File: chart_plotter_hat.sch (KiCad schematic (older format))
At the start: 65 parts, among them J1 JST PH, J10 JST PH, J2 JST PH, J3 40HAT, J4 JST PH, J5 JST PH, J6 JST PH, J7 JST PH, J8 Conn_02x03_Odd_Even, J9 JST PH, Q1 DMG2305UX, Q2 DMMT5401, Q3 DMG2305UX, U1 ATmega328P-AU, U2 CAT24C32, U3 MPM3610-5.0-adafruit, U4 LT1762-3.3, U5 G3VM-201FR, U6 MCP2515-xSO, U7 MCP2551-I-SN, U8 ST2378E, Y1 16MHz

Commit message: Added optical isolation in CAN
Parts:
- removed D1, D2: LED, LEDs:LED_0603, symbol Device:LED
- removed H5, H6: LightPipeMount, project_footprints:SMFLPX.X-light-pipe-adapter-smd, symbol CustomComponents:LightPipeMount
- removed J2: JST PH, Connectors_JST:JST_PH_B4B-PH-K_04x2.00mm_Straight, symbol Connector_Generic:Conn_01x04
- removed R3: 120, Resistors_SMD:R_0603, symbol Device:R
- removed R4: 300, Resistors_SMD:R_0603, symbol Device:R
- added C8, C9: .1uF, Capacitors_SMD:C_0603, symbol Device:C
- added J2: JST PH, Connectors_JST:JST_PH_B6B-PH-K_06x2.00mm_Straight, symbol Connector_Generic:Conn_01x06
- added U9: ADuM1201BR, Housings_SOIC:SOIC-8_3.9x4.9mm_Pitch1.27mm, symbol Isolator:ADuM1201BR
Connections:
- net labels added: LED_ACTION
- wire segments 245 -> 254
- no-connect marks 12 -> 23
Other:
- moved on the sheet: C12, C15, U7

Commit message: Redid CAN isolation, removed level shifter
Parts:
- removed C10: .1uF, Capacitors_SMD:C_0603, symbol Device:C
- removed Q3: DMG2305UX, TO_SOT_Packages_SMD:SOT-23, symbol raspberrypi_hat:DMG2305UX
- removed R12, R15, R5: 10K, Resistors_SMD:R_0603, symbol Device:R
- removed R14: 220, Resistors_SMD:R_0603, symbol Device:R
- removed U8: ST2378E, Housings_SSOP:TSSOP-20_4.4x6.5mm_Pitch0.65mm, symbol CustomComponents:ST2378E
- added C10: 10uF, Capacitors_Tantalum_SMD:CP_Tantalum_Case-A_EIA-3216-18_Reflow, symbol Device:CP
- added U8: LT1762-MS8, Housings_SSOP:MSOP-8_3x3mm_Pitch0.65mm, symbol CustomComponents:LT1762-MS8
- C11: value .1uF -> .01uF
- R11, R13, R16: value 10K -> 6.8K
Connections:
- net labels added: +5VP, GND2
- net labels removed: CCS, CRST, INT, MISO-2, MOSI-2, SCK-2, VEE_ENABLE
- wire segments 254 -> 225
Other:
- note added: "CAN Isolated Power"
- note removed: "3.3V Auxiliary"
- note removed: "VEE_ENABLE is active low to power auxiliary"
- moved on the sheet: C12, C15, C16, C17, C8, C9, J10, R11, R13, R16, U6, U7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

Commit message: Updated README
Created pdf of schematic, updated board graphic
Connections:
- net GND2 is gone; now on net GND: C10.2, C15.2, C9.2, U7.2 (VSS), U7.8 (Rs), U8.4 (GND), U8.7 (NC), U9.5 (GND2)
- net EN: no longer U8.5 (SHDN)
- net GND: now also U1.1 (PD3)
- net CAN_EN: now reaches U1.9 (PD5)
- net CAN_EN: now also U8.5 (SHDN)
- net CS renamed AVR_CS
- net LED_ACTION renamed LED1
- no-connect marks 23 -> 21
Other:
- note added: "HDWR IDENT"
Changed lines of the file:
@@
 	13100 5925 13375 5925
 Text GLabel 13375 5625 2    50   Input ~ 0
-CS
+AVR_CS
 Wire Wire Line
 	13100 5525 14950 5525
@@
 	2050 2375 1750 2375
 Text GLabel 3575 2375 2    50   Output ~ 0
-CS
+AVR_CS
 Wire Wire Line
 	3250 2375 3575 2375
@@
 MCU_RUNNING
 $Comp
-L Device:R R1
-U 1 1 5FEF7011
-P 14225 7575
-F 0 "R1" V 14305 7575 50  0000 C CNN
-F 1 "10K" V 14225 7575 50  0000 C CNN
-F 2 "Resistors_SMD:R_0603" V 14155 7575 50  0001 C CNN
-F 3 "" H 14225 7575 50  0001 C CNN
-	1    14225 7575
-	0    1    1    0
-$EndComp
-$Comp
-L power:+3.3V #PWR013
-U 1 1 5FF4180B
-P 14600 7575
-F 0 "#PWR013" H 14600 7425 50  0001 C CNN
-F 1 "+3.3V" H 14615 7748 50  0000 C CNN
-F 2 "" H 14600 7575 50  0001 C CNN
-F 3 "" H 14600 7575 50  0001 C CNN
-	1    14600 7575
-	1    0    0    -1
-$EndComp
-$Comp
 L Device:C C5
 U 1 1 5FFED6E8
@@
 	1750 3075 2050 3075
 NoConn ~ 13100 7725
-NoConn ~ 13100 7625
-NoConn ~ 13100 7425
 NoConn ~ 13100 7225
 NoConn ~ 13100 7125
@@
 $EndComp
 Text GLabel 14525 4500 0    50   Output ~ 0
-LED_ACTION
+LED1
 Text GLabel 13675 5425 2    50   Output ~ 0
-LED_ACTION
+LED1
 Wire Wire Line
 	13100 5425 13675 5425
@@
 L power:+5VP #PWR017
 U 1 1 612C4211
-P 6950 6600
-F 0 "#PWR017" H 6950 6450 50  0001 C CNN
-F 1 "+5VP" H 6965 6773 50  0000 C CNN
-F 2 "" H 6950 6600 50  0001 C CNN
-F 3 "" H 6950 6600 50  0001 C CNN
-	1    6950 6600
+P 7125 6600
+F 0 "#PWR017" H 7125 6450 50  0001 C CNN
+F 1 "+5VP" H 7140 6773 50  0000 C CNN
+F 2 "" H 7125 6600 50  0001 C CNN
+F 3 "" H 7125 6600 50  0001 C CNN
+	1    7125 6600
 	1    0    0    -1
 $EndComp
@@
 	6950 6900 6950 7350
 Text GLabel 5125 7000 0    50   Input ~ 0
-EN
+CAN_EN
 Wire Wire Line
 	5125 7000 5250 7000
@@
 Wire Wire Line
 	6050 7350 6950 7350
+$Comp
+L power:GND2 #PWR0127
+U 1 1 6123FC34
+P 14625 4600
+F 0 "#PWR0127" H 14625 4350 50  0001 C CNN
+F 1 "GND2" H 14630 4427 50  0000 C CNN
+F 2 "" H 14625 4600 50  0001 C CNN
+F 3 "" H 14625 4600 50  0001 C CNN
+	1    14625 4600
+	1    0    0    -1
+$EndComp
+Wire Wire Line
+	14625 4600 14850 4600
+Connection ~ 14850 4600
+Text GLabel 13375 7625 2    50   Output ~ 0
+CAN_EN
+Wire Wire Line
+	13100 7625 13375 7625
+$Comp
+L power:+3.3V #PWR013
+U 1 1 5FF4180B
+P 14600 7575
+F 0 "#PWR013" H 14600 7425 50  0001 C CNN
+F 1 "+3.3V" H 14615 7748 50  0000 C CNN
+F 2 "" H 14600 7575 50  0001 C CNN
+F 3 "" H 14600 7575 50  0001 C CNN
+	1    14600 7575
+	1    0    0    -1
+$EndComp
+$Comp
+L Device:R R1
+U 1 1 5FEF7011
+P 14225 7575
+F 0 "R1" V 14305 7575 50  0000 C CNN
+F 1 "10K" V 14225 7575 50  0000 C CNN
+F 2 "Resistors_SMD:R_0603" V 14155 7575 50  0001 C CNN
+F 3 "" H 14225 7575 50  0001 C CNN
+	1    14225 7575
+	0    1    1    0
+$EndComp
+Text Notes 13425 7425 0    50   ~ 0
+HDWR IDENT
+$Comp
+L power:GND #PWR?
+U 1 1 612417F0
+P 13925 7425
+F 0 "#PWR?" H 13925 7175 50  0001 C CNN
+F 1 "GND" H 13925 7275 50  0000 C CNN
+F 2 "" H 13925 7425 50  0000 C CNN
+F 3 "" H 13925 7425 50  0000 C CNN
+	1    13925 7425
+	1    0    0    -1
+$EndComp
+Wire Wire Line
+	13100 7425 13925 7425
+Wire Wire Line
+	6950 6600 7125 6600
 $EndSCHEMATC

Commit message: Added power isolation to CAN
TVS added to CAN output
DCP01B used for power isolation from board
Another LT1762 used for CAN isolation power
Removed pull-ups from CAN controller, should be controlled by Pi
Added LED's for hat pwr, pi pwr, CAN isolation pwr, and CAN Rx
Reordered connections on Power connector
Added CAN gnd isolation pin on CAN connector
No more CAN_EN, as it is covered by isolation hookup
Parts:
- removed J10: JST PH, Connectors_JST:JST_PH_B2B-PH-K_02x2.00mm_Straight, symbol Connector_Generic:Conn_01x02
- removed R11, R13, R16: 6.8K, Resistors_SMD:R_0603, symbol Device:R
- added C13: 1uF, Capacitors_SMD:C_1206, symbol Device:C
- added C14: 2.2uF, Capacitors_SMD:C_1206, symbol Device:C
- added D2, D3, D4: RED, Diodes_SMD:D_0603, symbol Device:LED
- added D5: GRN, Diodes_SMD:D_0603, symbol Device:LED
- added J10: JST PH, Connectors_JST:JST_PH_B3B-PH-K_03x2.00mm_Straight, symbol Connector_Generic:Conn_01x03
- added R12: 300, Resistors_SMD:R_0603, symbol Device:R
- added R3, R5: 390, Resistors_SMD:R_0603, symbol Device:R
- added R4: 180, Resistors_SMD:R_0603, symbol Device:R
- added U10: DCP01B, CustomComponents:DCP01B_SO_7_14, symbol CustomComponents:DCP01B
- added U11: VCAN26A2, TO_SOT_Packages_SMD:SOT-323_SC-70, symbol CustomComponents:VCAN26A2
- renumbered D3 to D1
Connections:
- net +12V: no longer U8.8 (Vin)
- net +3V3: now also D3.2 (A)
- net +5V: now also J2.3 (Pin_3), J2.5 (Pin_5), C14.1, D2.2 (A), U10.1 (Vs); no longer J2.2 (Pin_2), J2.4 (Pin_4)
- net +5VP: now also D4.2 (A)
- net BUTTON: now also J2.4 (Pin_4); no longer J2.3 (Pin_3)
- net CAN_HI: now also J10.1 (Pin_1), U11.2
- net CAN_LO: now also J10.2 (Pin_2), U11.1
- net GND: now also J2.2 (Pin_2), C14.2, R3.1, R4.1, U10.2 (0V); no longer C10.2, C15.2, C9.2, J2.6 (Pin_6), U7.2 (VSS), U7.8 (Rs), U8.4 (GND), U8.7 (NC), U9.5 (GND2)
- net LED1: now also J2.6 (Pin_6); no longer J2.5 (Pin_5)
- net at U7.4 (RXD), U9.7 (VIA): now also D5.2 (A)
- net CAN_EN: no longer names the net of U1.9 (PD5)
- net CAN_EN: no longer U8.5 (SHDN)
- new net: C13.1, U10.6 (Vout), U8.5 (SHDN), U8.8 (Vin)
- new net: D2.1 (K), R3.2
- new net: D3.1 (K), R4.2
- new net: D4.1 (K), R5.2
- new net: D5.1 (K), R12.2
- new net GND2: C10.2, C13.2, C15.2, C9.2, J10.3 (Pin_3), R12.1, R5.1, U10.5 (0V), U11.3, U7.2 (VSS), U7.8 (Rs), U8.4 (GND), U9.5 (GND2)
- no-connect marks 21 -> 25
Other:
- note added: "CAN Connector"
- moved on the sheet: C10, C11, C12, C15, C16, C17, C8, C9, U6, U7, U8, U9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

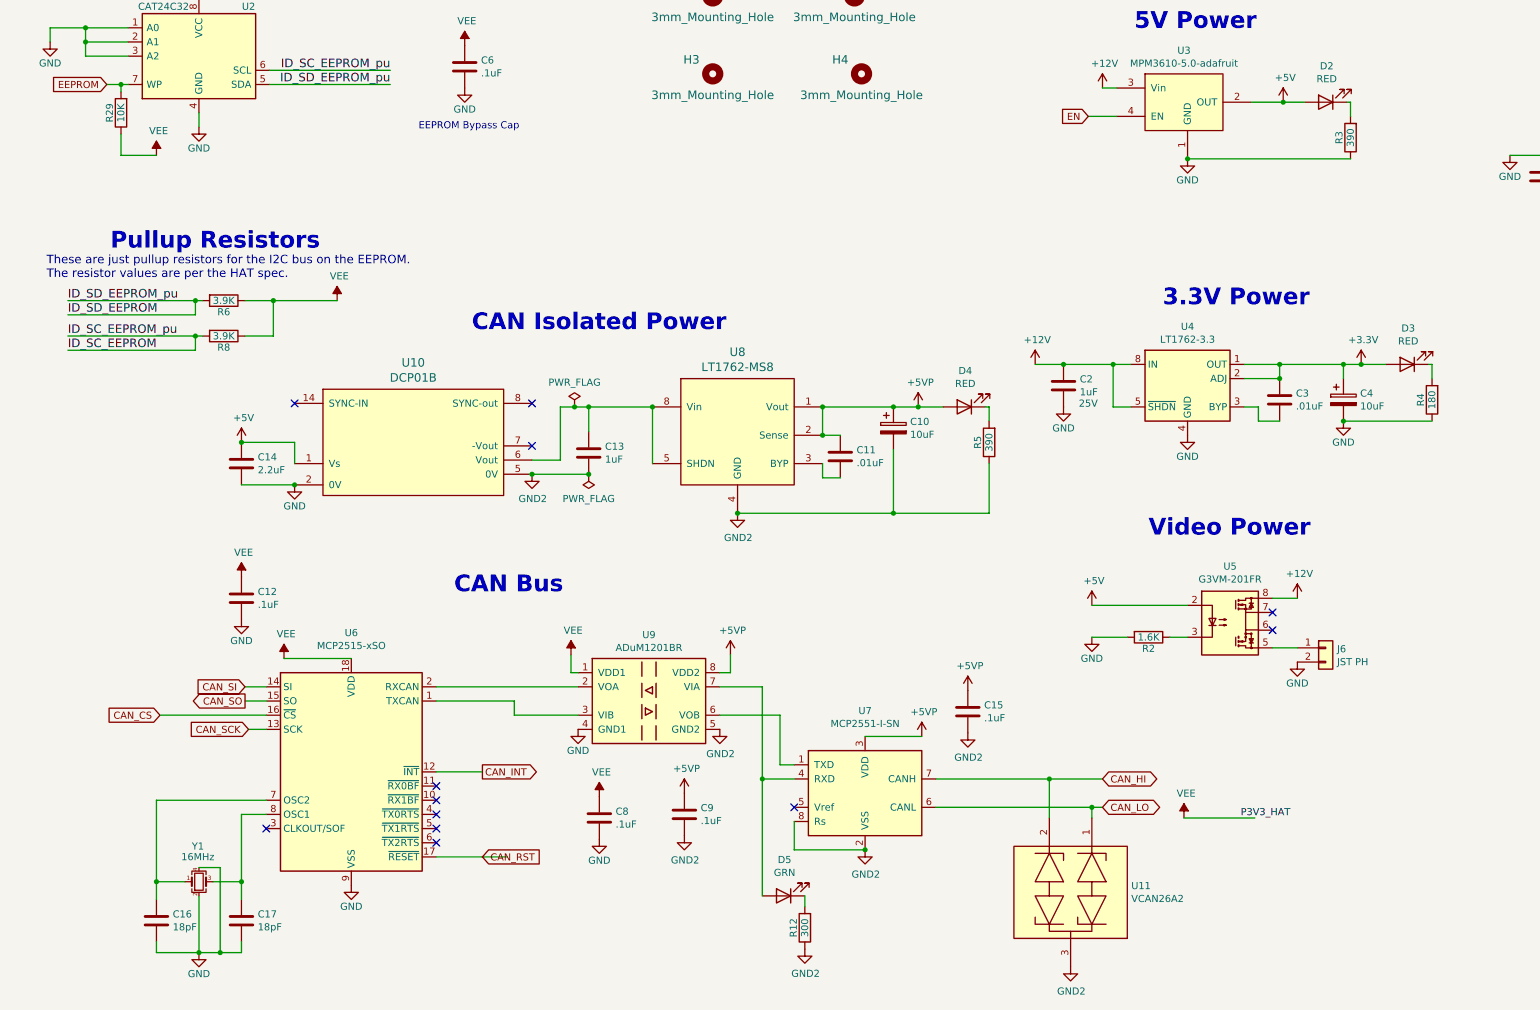
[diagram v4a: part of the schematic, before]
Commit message: Renamed some resistors
Changed resistor value from 180 to 220, to match inventory
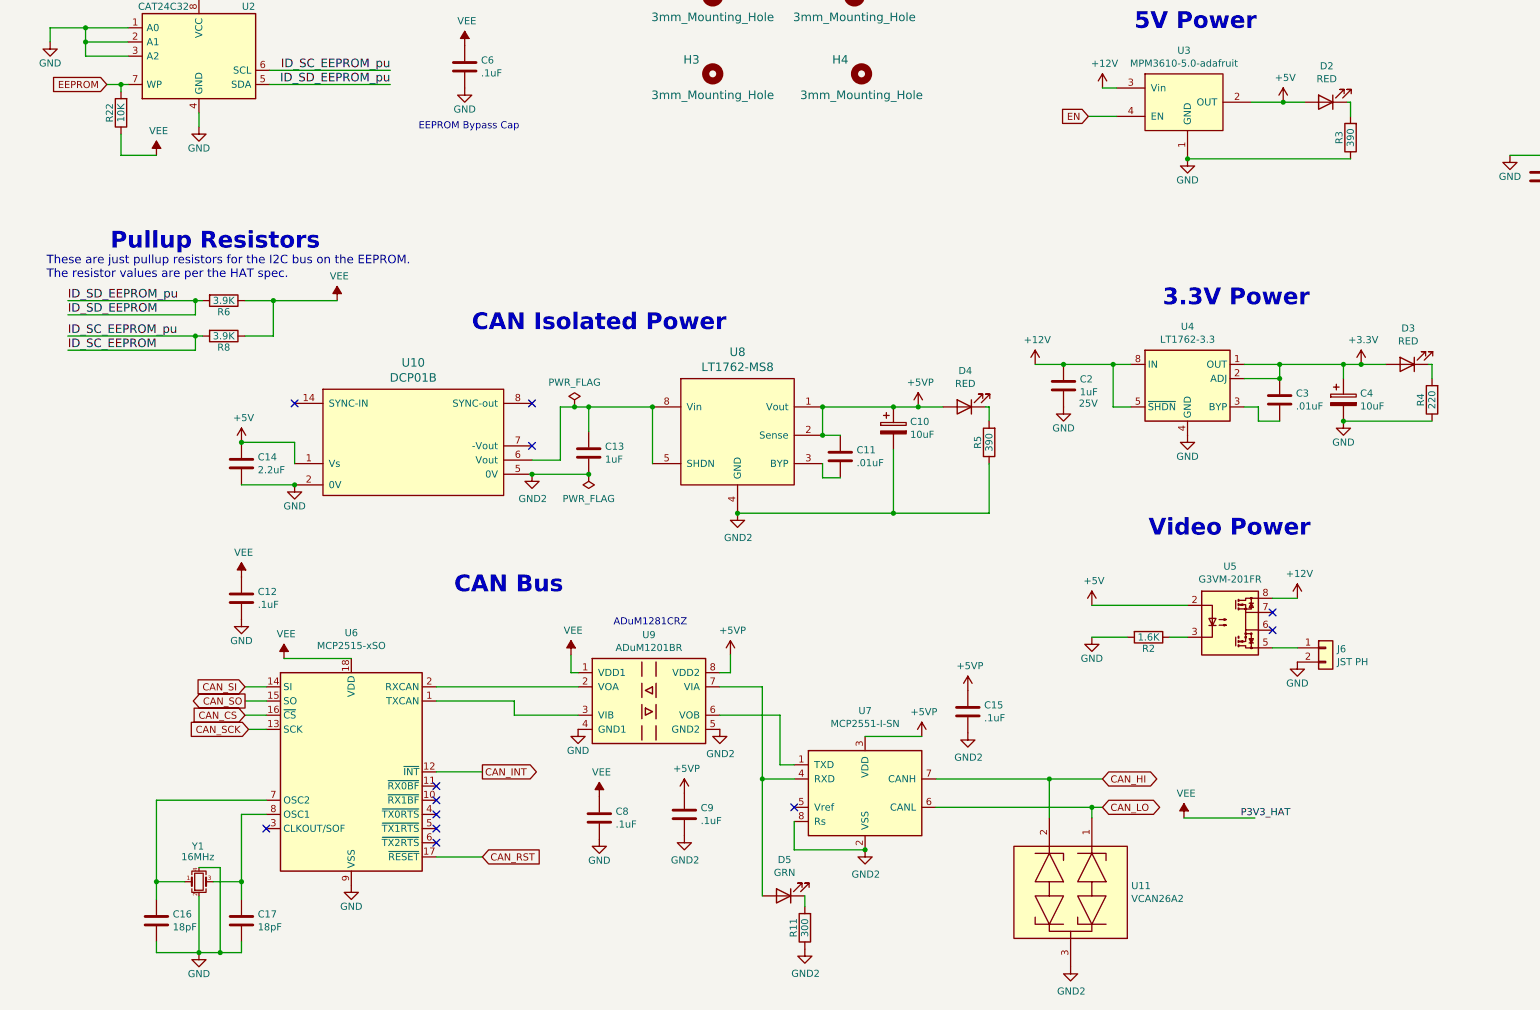
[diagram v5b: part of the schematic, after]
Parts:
- R4: value 180 -> 220
- renumbered R12 to R11, R29 to R22
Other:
- note added: "ADuM1281CRZ"
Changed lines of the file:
@@
 ID_SC_EEPROM_pu
 $Comp
-L Device:R R29
+L Device:R R22
 U 1 1 58E19E51
 P 1600 4825
-F 0 "R29" V 1680 4825 50  0000 C CNN
+F 0 "R22" V 1680 4825 50  0000 C CNN
 F 1 "10K" V 1600 4825 50  0000 C CNN
 F 2 "Resistors_SMD:R_0603" V 1530 4825 50  0001 C CNN
@@
 Wire Wire Line
 	3600 3175 3250 3175
-Text GLabel 1875 9075 0    50   Input ~ 0
+Text GLabel 2475 9075 0    50   Input ~ 0
 CAN_CS
 Text GLabel 3600 1775 2    50   Input ~ 0
@@
 P 10850 6850
 F 0 "R4" V 10930 6850 50  0000 C CNN
-F 1 "180" V 10850 6850 50  0000 C CNN
+F 1 "220" V 10850 6850 50  0000 C CNN
 F 2 "Resistors_SMD:R_0603" V 10780 6850 50  0001 C CNN
 F 3 "" H 10850 6850 50  0001 C CNN
@@
 $EndComp
 $Comp
-L Device:R R12
+L Device:R R11
 U 1 1 61810910
 P 6425 10575
-F 0 "R12" V 6505 10575 50  0000 C CNN
+F 0 "R11" V 6505 10575 50  0000 C CNN
 F 1 "300" V 6425 10575 50  0000 C CNN
 F 2 "Resistors_SMD:R_0603" V 6355 10575 50  0001 C CNN
@@
 Connection ~ 4900 7375
 Wire Wire Line
-	1875 9075 2625 9075
-Wire Wire Line
-	3825 10075 4325 10075
-Wire Wire Line
 	3825 9475 4150 9475
 Wire Wire Line
@@
 Wire Wire Line
 	14075 4200 14850 4200
+Wire Wire Line
+	3825 10075 4150 10075
+Wire Wire Line
+	2475 9075 2625 9075
+Text Notes 5075 8450 0    50   ~ 0
+ADuM1281CRZ
 $EndSCHEMATC

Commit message: Updated schematic pdf
Changed drawing size to US Ledger, instead of A3
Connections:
- net GND2: now also U8.7 (NC)
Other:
- note added: "Isolated CAN Power"
- note removed: "CAN Isolated Power"
- moved on the sheet: C1, C10, C11, C12, C13, C14, C15, C16, C17, C2, C3, C4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
